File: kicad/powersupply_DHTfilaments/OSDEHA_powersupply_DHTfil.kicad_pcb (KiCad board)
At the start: 2 copper layers, 28 parts, among them J1 10.5 VAC / 4.5 A, J2 10.5 VAC / 4.5 A, J3 COLEMANREG-LEFT-1, J4 COLEMANREG-LEFT-2, J5 COLEMANREG-RIGHT-1, J6 COLEMANREG-RIGHT-2

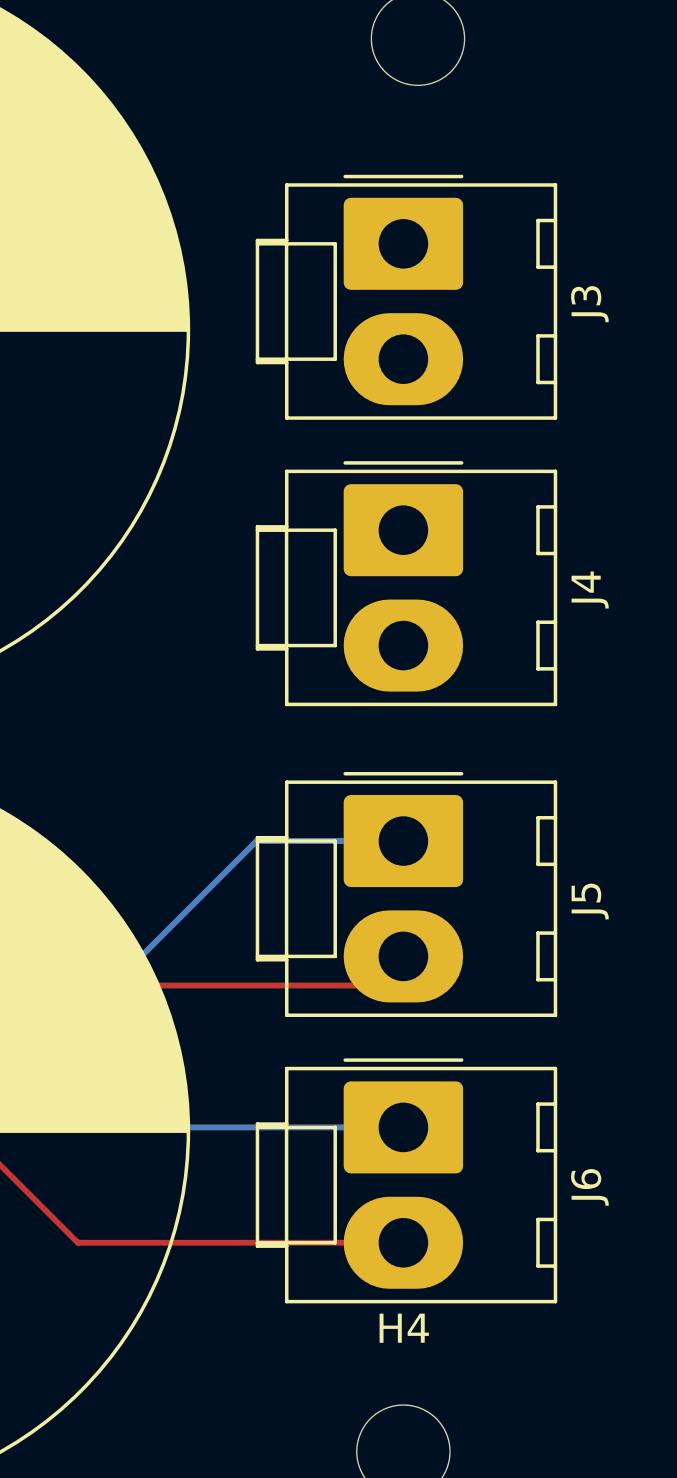
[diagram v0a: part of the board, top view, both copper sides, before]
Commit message: improved + simplified wiring/connections to DHT filaments, improved pin/net labels
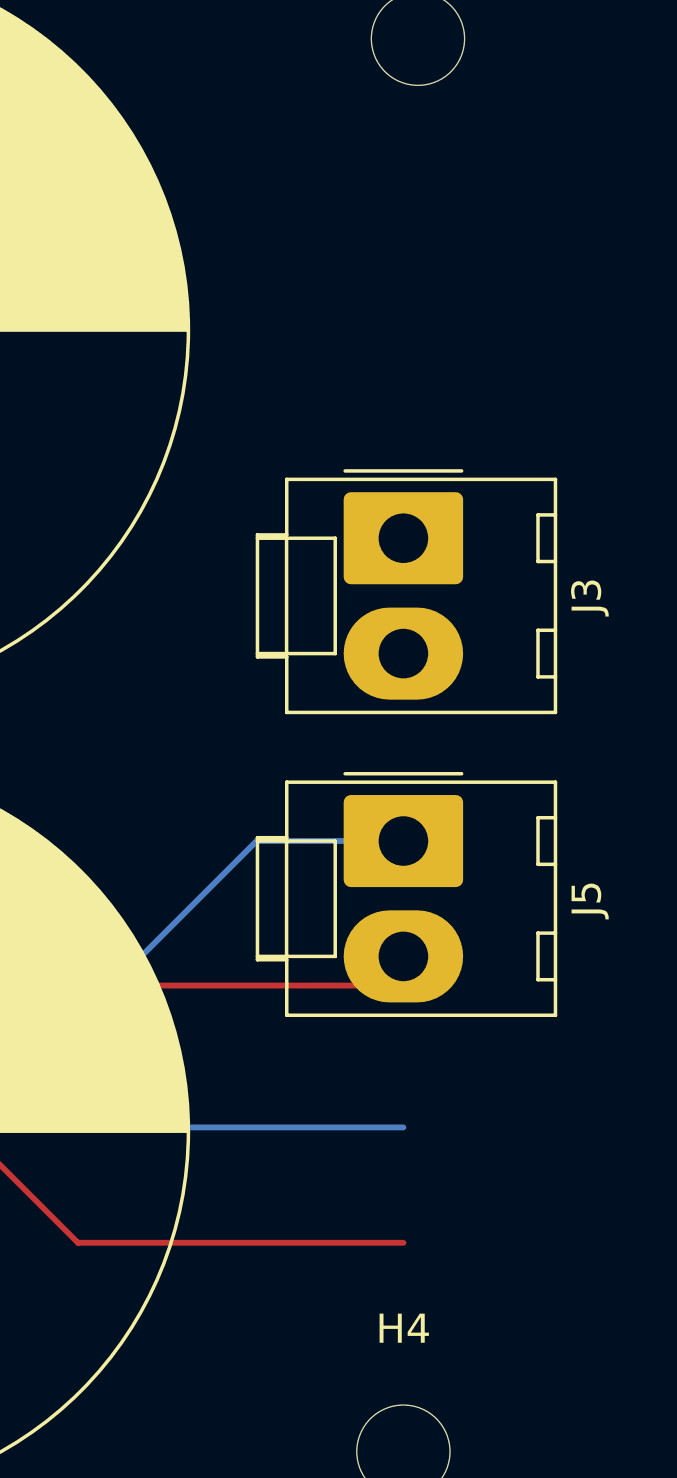
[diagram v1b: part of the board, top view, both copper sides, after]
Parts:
- removed J4: COLEMANREG-LEFT-2, Connector_Molex:Molex_KK-396_A-41791-0002_1x02_P3.96mm_Vertical
- removed J6: COLEMANREG-RIGHT-2, Connector_Molex:Molex_KK-396_A-41791-0002_1x02_P3.96mm_Vertical
- J3: value COLEMANREG-LEFT-1 -> 2 x COLEMANREG-LEFT
- J5: value COLEMANREG-RIGHT-1 -> 2 x COLEMANREG-RIGHT
- moved J3 10.1 mm to (188.5, 73.5)

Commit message: added pin labels
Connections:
- net /COLEMAN_RAW_DC_LEFT/RAWDC+ renamed /RAWDC_L+
- net /COLEMAN_RAW_DC_LEFT/RAWDC- renamed /RAWDC_L-
- net /COLEMAN_RAW_DC_RIGHT/RAWDC+ renamed /RAWDC_R+
- net /COLEMAN_RAW_DC_RIGHT/RAWDC- renamed /RAWDC_R-
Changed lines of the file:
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@@
 	(net 1 "Net-(D1-K)")
 	(net 2 "Net-(D2-A)")
-	(net 3 "/COLEMAN_RAW_DC_LEFT/RAWDC-")
-	(net 4 "/COLEMAN_RAW_DC_LEFT/RAWDC+")
+	(net 3 "/RAWDC_L-")
+	(net 4 "/RAWDC_L+")
 	(net 5 "Net-(D6-A)")
 	(net 6 "Net-(D5-K)")
-	(net 7 "/COLEMAN_RAW_DC_RIGHT/RAWDC+")
-	(net 8 "/COLEMAN_RAW_DC_RIGHT/RAWDC-")
+	(net 7 "/RAWDC_R+")
+	(net 8 "/RAWDC_R-")
 	(net 9 "/COLEMAN_RAW_DC_LEFT/AC1")
 	(net 10 "/COLEMAN_RAW_DC_LEFT/AC2")
@@
 			(remove_unused_layers no)
 			(roundrect_rratio 0.079114)
-			(net 4 "/COLEMAN_RAW_DC_LEFT/RAWDC+")
+			(net 4 "/RAWDC_L+")
 			(pinfunction "Pin_1")
 			(pintype "passive")
@@
 			(layers "*.Cu" "*.Mask")
 			(remove_unused_layers no)
-			(net 3 "/COLEMAN_RAW_DC_LEFT/RAWDC-")
+			(net 3 "/RAWDC_L-")
 			(pinfunction "Pin_2")
 			(pintype "passive")
@@
 			(layers "*.Cu" "*.Mask")
 			(remove_unused_layers no)
-			(net 7 "/COLEMAN_RAW_DC_RIGHT/RAWDC+")
+			(net 7 "/RAWDC_R+")
 			(pintype "passive")
 		)
@@
 			(layers "*.Cu" "*.Mask")
 			(remove_unused_layers no)
-			(net 3 "/COLEMAN_RAW_DC_LEFT/RAWDC-")
+			(net 3 "/RAWDC_L-")
 			(pintype "passive")
 		)
@@
 			(remove_unused_layers no)
 			(roundrect_rratio 0.079114)
-			(net 7 "/COLEMAN_RAW_DC_RIGHT/RAWDC+")
+			(net 7 "/RAWDC_R+")
 			(pinfunction "Pin_1")
 			(pintype "passive")
@@
 			(layers "*.Cu" "*.Mask")
 			(remove_unused_layers no)
-			(net 8 "/COLEMAN_RAW_DC_RIGHT/RAWDC-")
+			(net 8 "/RAWDC_R-")
 			(pinfunction "Pin_2")
 			(pintype "passive")
@@
 			(layers "*.Cu" "*.Mask")
 			(remove_unused_layers no)
-			(net 4 "/COLEMAN_RAW_DC_LEFT/RAWDC+")
+			(net 4 "/RAWDC_L+")
 			(pintype "passive")
 		)
@@
 			(layers "*.Cu" "*.Mask")
 			(remove_unused_layers no)
-			(net 8 "/COLEMAN_RAW_DC_RIGHT/RAWDC-")
+			(net 8 "/RAWDC_R-")
 			(pintype "passive")
 		)
@@
 			(layers "*.Cu" "*.Mask")
 			(remove_unused_layers no)
-			(net 7 "/COLEMAN_RAW_DC_RIGHT/RAWDC+")
+			(net 7 "/RAWDC_R+")
 			(pintype "passive")
 		)
@@
 			(layers "*.Cu" "*.Mask")
 			(remove_unused_layers no)
-			(net 8 "/COLEMAN_RAW_DC_RIGHT/RAWDC-")
+			(net 8 "/RAWDC_R-")
 			(pintype "passive")
 		)
@@
 			(layers "*.Cu" "*.Mask")
 			(remove_unused_layers no)
-			(net 4 "/COLEMAN_RAW_DC_LEFT/RAWDC+")
+			(net 4 "/RAWDC_L+")
 			(pintype "passive")
 		)
@@
 			(layers "*.Cu" "*.Mask")
 			(remove_unused_layers no)
-			(net 3 "/COLEMAN_RAW_DC_LEFT/RAWDC-")
+			(net 3 "/RAWDC_L-")
 			(pintype "passive")
 		)

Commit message: work on DC raw supply PCB
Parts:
- removed C3, C4: 15000u 25 V, Capacitor_THT:CP_Radial_D25.0mm_P10.00mm_SnapIn
- removed D5, D6, D7, D8: 1N5822, Diode_THT:D_DO-201AD_P15.24mm_Horizontal
- removed J1, J2: 10.5 VAC / 4.5 A, TerminalBlock_Phoenix:TerminalBlock_Phoenix_MKDS-1,5-2-5.08_1x02_P5.08mm_Horizontal
- removed J3: 2 x COLEMANREG-LEFT, Connector_Molex:Molex_KK-396_A-41791-0002_1x02_P3.96mm_Vertical
- removed J5: 2 x COLEMANREG-RIGHT, Connector_Molex:Molex_KK-396_A-41791-0002_1x02_P3.96mm_Vertical
- removed R4: 10k, Resistor_THT:R_Axial_DIN0207_L6.3mm_D2.5mm_P2.54mm_Vertical
- removed R5, R6: 0.22 3 W, Resistor_THT:R_Axial_DIN0614_L14.3mm_D5.7mm_P5.08mm_Vertical
- added AC1: 10.5 VAC / 4.5 A, TerminalBlock_Phoenix:TerminalBlock_Phoenix_MKDS-1,5-2-5.08_1x02_P5.08mm_Horizontal, F.Cu at (75.8, 84.0)
- added DC1: 2 x COLEMANREGs, Connector_Molex:Molex_KK-396_A-41791-0002_1x02_P3.96mm_Vertical, F.Cu at (162.5, 79.5)
- R2, R3: footprint Resistor_THT:R_Axial_DIN0614_L14.3mm_D5.7mm_P5.08mm_Vertical -> Resistor_THT:R_Axial_DIN0414_L11.9mm_D4.5mm_P5.08mm_Vertical
- moved H2 118.7 mm to (75.5, 91.1)
- moved H3 69.4 mm to (162.6, 71.9)
- moved R3 45.4 mm to (129.0, 92.0), turned to 90 degrees
- moved D3 42.6 mm to (83.8, 84.9), turned to 0 degrees
- moved D4 39.2 mm to (83.8, 91.6)
- moved H4 29.4 mm to (162.6, 91.1)
- moved H1 28.6 mm to (75.5, 71.9)
- moved C1 27.5 mm to (114.5, 76.5), turned to -90 degrees
- moved R2 26.8 mm to (129.0, 70.9), turned to -90 degrees
- moved D1 26.6 mm to (99.0, 71.4)
- moved C2 25.5 mm to (143.5, 76.5), turned to -90 degrees
- moved R1 25.1 mm to (129.0, 80.0)
- moved D2 24.8 mm to (99.0, 78.1), turned to 180 degrees
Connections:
- net /RAWDC_L+ renamed /DC+
- net /RAWDC_L- renamed /DC-
- C1 pad 1: Net-(D1-K) -> /R+
- C1 pad 2: Net-(D2-A) -> /R-
- D1 pad 1: Net-(D1-K) -> /R+
- D1 pad 2: /COLEMAN_RAW_DC_LEFT/AC1 -> /AC1
- D2 pad 1: /COLEMAN_RAW_DC_LEFT/AC1 -> /R+
- D2 pad 2: Net-(D2-A) -> /AC2
- D3 pad 1: Net-(D1-K) -> /AC1
- D3 pad 2: /COLEMAN_RAW_DC_LEFT/AC2 -> /R-
- D4 pad 1: /COLEMAN_RAW_DC_LEFT/AC2 -> /AC2
- D4 pad 2: Net-(D2-A) -> /R-
- R1 pad 1: Net-(D1-K) -> /R+
- R1 pad 2: Net-(D2-A) -> /R-
- R2 pad 1: Net-(D1-K) -> /R+
- R3 pad 1: Net-(D2-A) -> /R-
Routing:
- net /RAWDC_R-: track 59.0 -> 0.00 mm
- net /RAWDC_R+: track 55.1 -> 0.00 mm
- net Net-(D6-A): track 52.8 -> 0.00 mm
- net Net-(D5-K): track 43.3 -> 0.00 mm
- net Net-(D2-A): track 39.1 -> 0.00 mm
- net Net-(D1-K): track 38.7 -> 0.00 mm
- net /AC1: track 0.00 -> 30.3 mm
- net /AC2: track 0.00 -> 29.6 mm
- net /COLEMAN_RAW_DC_RIGHT/AC1: track 27.5 -> 0.00 mm
- net /COLEMAN_RAW_DC_RIGHT/AC2: track 26.7 -> 0.00 mm
- net /R+: track 0.00 -> 22.3 mm
- net /R-: track 0.00 -> 20.1 mm
- net /DC-: track 14.1 -> 9.18 mm
- net /DC+: track 13.9 -> 9.44 mm
- added copper zone on B.Cu, net /DC+
- added copper zone on B.Cu, net /DC-
- added copper zone on B.Cu, net /R+
- added copper zone on B.Cu, net /R-
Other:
- board outline added: 98.5 x 26.5 mm

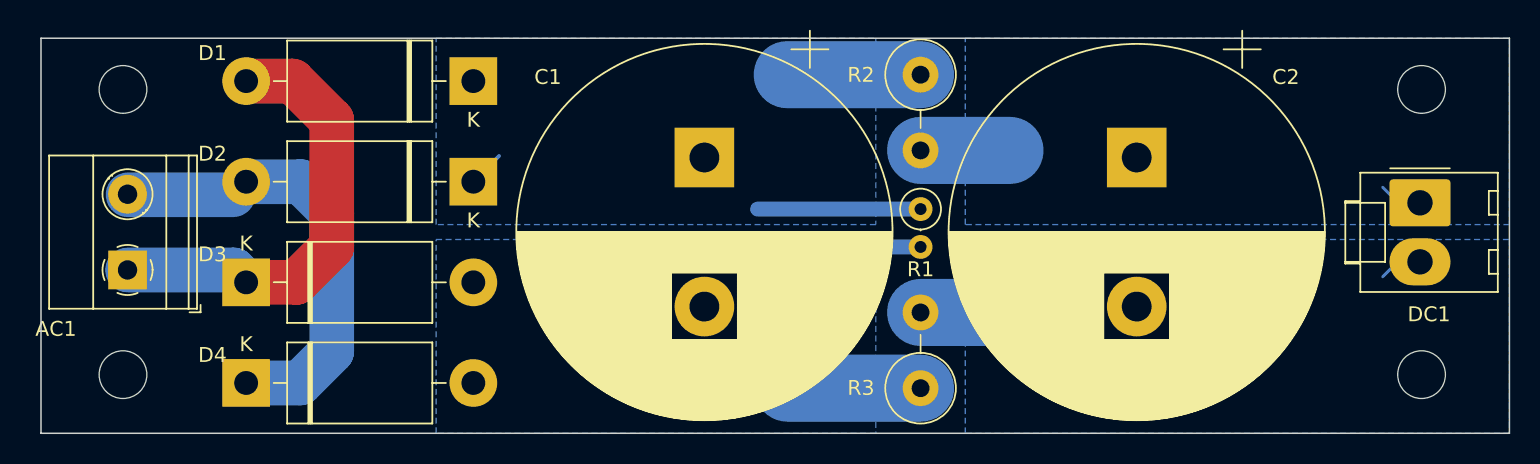
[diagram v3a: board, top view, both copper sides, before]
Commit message: use same clearance on filled zones for all PCBs
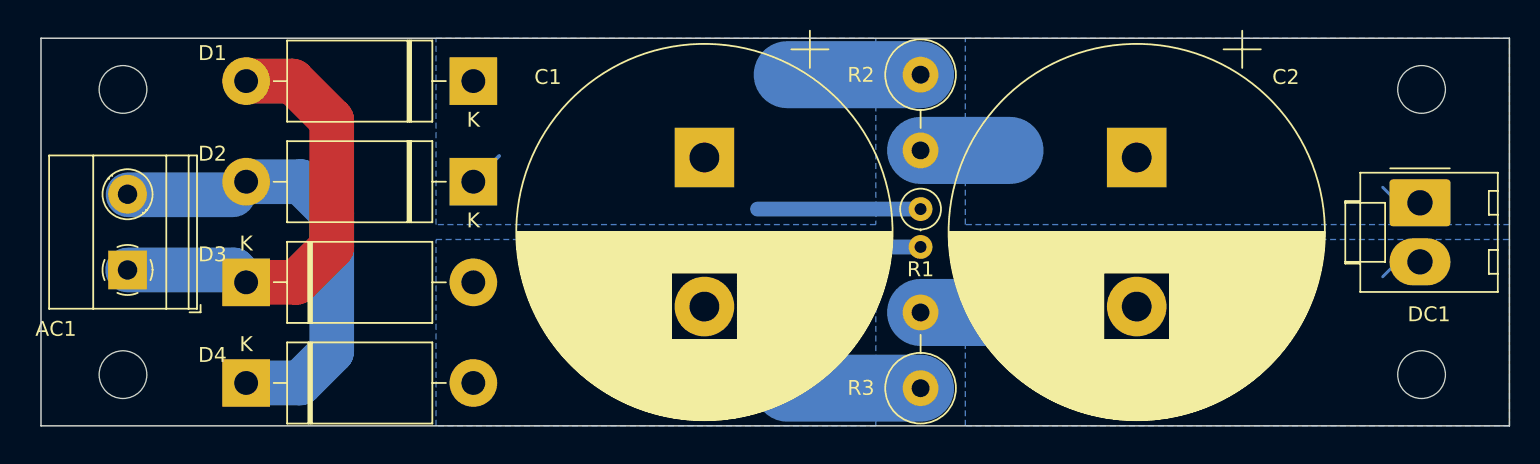
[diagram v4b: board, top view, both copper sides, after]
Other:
- board size 98.5 x 26.5 mm -> 98.5 x 26 mm
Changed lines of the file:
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@@
 	(gr_line
 		(start 168.5 68.5)
-		(end 168.5 95)
+		(end 168.5 94.5)
 		(stroke
 			(width 0.1)
@@
 	)
 	(gr_line
-		(start 168.5 95)
-		(end 70 95)
+		(start 168.5 94.5)
+		(end 70 94.5)
 		(stroke
 			(width 0.1)
@@
 	)
 	(gr_line
-		(start 70 95)
+		(start 70 94.5)
 		(end 70 68.5)
 		(stroke
@@
 		(hatch edge 0.5)
 		(connect_pads
-			(clearance 0.5)
+			(clearance 1)
 		)
 		(min_thickness 0.25)
@@
 		(polygon
 			(pts
-				(xy 168.5 82) (xy 168.5 95) (xy 132 95) (xy 132 82)
+				(xy 168.5 82) (xy 168.5 94.5) (xy 132 94.5) (xy 132 82)
 			)
 		)
@@
 		(hatch edge 0.5)
 		(connect_pads
-			(clearance 0.5)
+			(clearance 1)
 		)
 		(min_thickness 0.25)
@@
 		(polygon
 			(pts
-				(xy 126 82) (xy 126 95) (xy 96.5 95) (xy 96.5 82)
+				(xy 126 82) (xy 126 94.5) (xy 96.5 94.5) (xy 96.5 82)
 			)
 		)
@@
 		(hatch edge 0.5)
 		(connect_pads
-			(clearance 0.5)
+			(clearance 1)
 		)
 		(min_thickness 0.25)
@@
 		(hatch edge 0.5)
 		(connect_pads
-			(clearance 0.5)
+			(clearance 1)
 		)
 		(min_thickness 0.25)

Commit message: PCB layout work
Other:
- board text added: "mbrennwa.github.io/OSDEHA"
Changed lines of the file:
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@@
 		(layer "Edge.Cuts")
+	)
+	(gr_text "mbrennwa.github.io/OSDEHA"
+		(at 158.25 93.65 0)
+		(layer "B.SilkS")
+		(effects
+			(font
+				(size 1.15 1.15)
+				(thickness 0.15)
+			)
+			(justify left bottom mirror)
+		)
 	)
 	(segment

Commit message: minor clean
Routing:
- net /R+: track 22.3 -> 19.9 mm
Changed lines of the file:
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@@
-	)
-	(segment
-		(start 100.73037 76.39463)
-		(end 99 78.125)
-		(width 0.25)
-		(layer "B.Cu")
-		(net 5)
 	)
 	(segment
